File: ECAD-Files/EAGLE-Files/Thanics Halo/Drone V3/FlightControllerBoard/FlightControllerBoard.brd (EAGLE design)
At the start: 60 x 80 mm, 92 parts, among them J12 UE27AE54100, J4 UE27AE54100, J5 U.FL, J7 62674-301121ALF, J8 MICROSD, U3 MPL115A2, U4 NEO-M8, U5 VL53L1

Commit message: Finished overall board zoning and component placement
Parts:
- removed C19, C22, C7, C8: 16pF, 16pF-capacitor:G-155-M
- removed J6: (no value), thanics_robotics:JST_SH_2POS
- removed R32: 20R, 20-resistor:RC0603N-M
- removed U5: VL53L1, thanics_robotics:VL53L1
- added C1, C12: 0.1uF, 0.1uF-capacitor-0402:0402-M
- added D2, D3, D4: GREEN, SparkFun-LED:LED-0603
- added J10, J11, J15, J16, J17, J18, J19, J20, J21, J22, J9: (no value), thanics_robotics:JST_SH_4POS
- added JP1: (no value), pinhead:2X06
- added L4: 1000R, 600ohm-fb:IND_BLM18_0603-M
- added R24, R25, R26, R27: 49R9, 49.9-resistor:RC0402N-M
- added R28, R30, R31: 1k, 1k-resistor:RC0603N-M
- added R29: 10k, 10k-resistor(0603):RC0603N-M
- C41: value 0.1uF -> 22uF; device 0.1uF-capacitor-0402:0402-M -> 22uF X5R Ceramic Capacitor:G-21
- C42: value 4.7uF -> 10uF; device 4.7uF-capacitor:0603-M -> 10uF X5R Ceramic Capacitor:G-21
- R10, R11, R13, R14, R2: device 10k-resistor:RC0805N -> 10k-resistor(0603):RC0603N-M
- R19: value 10k -> 1k; device 10k-resistor:RC0805N -> 1k-resistor:RC0603N-M
- moved R10 364.1 mm to (-86.3, -281.3)
- moved R13 360.1 mm to (-86.3, -278.4)
- moved R11 357.8 mm to (-86.3, -275.5)
- moved J1 308.4 mm to (4.32, 68.8)
- moved J2 294.7 mm to (4.37, 63.4)
- moved U$2 293.6 mm to (24.4, 44.6), turned to 180 degrees
- moved R2 201.8 mm to (-86.3, -272.6)
- moved C16 158.5 mm to (37.5, 30.1), flipped to the bottom
- moved R20 158.2 mm to (32.3, 32.4), flipped to the bottom, turned to 315 degrees
- moved C15 157.9 mm to (36.6, 26.2)
- moved R21 152.5 mm to (28.8, 31.9), flipped to the bottom, turned to 225 degrees
- moved C17 150.8 mm to (32.5, 27.8), turned to 90 degrees
- moved C25 146.6 mm to (30.2, 27.8), turned to 90 degrees
- moved R4 140.8 mm to (26.8, 29.1)
- moved C6 139.8 mm to (34.3, 26.5), turned to 90 degrees
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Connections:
- removed net BATT_SCL: J7.20
- removed net BATT_SDA: J7.19
- removed net GPCLK: U2.61
- removed net N$17: U6.60
- new net ETH_BIAS: C1.2, L4.2, U$1.13
- new net GND1: D2.C, U$1.60
- new net GND2: D3.C
- new net GPIO12: JP1.1, U6.45
- new net GPIO13: JP1.3, U6.47
- new net GPIO16: JP1.5, U6.57
- new net GPIO17: JP1.2, U6.59
- new net GPIO37: JP1.4, U6.60
- new net GPIO38: JP1.6, U6.64
- new net GPIO39: JP1.8, U6.66
- new net N$22: D3.A, R30.1
- new net N$23: C12.2, L4.1, R24.1, R25.1, R26.1, R27.1
- new net N$24: R2.2, U$1.15
- new net N$25: D4.A, U$1.11
- new net N$27: D4.C, R31.1
- net +3V3: now also C42.1, J10.1, J11.1, J15.1, J16.1, J17.1, J18.1, J19.1, J20.1, J21.1, J22.1, J9.1, JP1.11, R19.2, R29.2, R30.2, U$1.61, U$1.62, U$2.16, U$2.6; no longer C41.2, C42.2, R19.1, R2.2, R32.2, U5.1, U5.11
- net +5V: now also C41.1, JP1.12, U$1.63, U$1.64; no longer J6.1
- net 3.3V_A: now also R2.1, R28.2
- net GND: now also C1.1, C12.1, C41.2, C42.2, J10.4, J11.4, J15.4, J16.4, J17.4, J18.4, J19.4, J20.4, J21.4, J22.4, J9.4, JP1.10, R31.2, U$1.1, U$1.17, U$1.25, U$1.26, U$1.39, U$1.40, U$2.7, U$2.8; no longer C19.1, C22.1, C41.1, C42.1, C7.1, C8.1, J6.2, U5.12, U5.2, U5.3, U5.4, U5.6
- net GPCLK1: now also U2.61
- net I2C_SCL: now also J10.3, J11.3, J15.3, J16.3, J17.3, J18.3, J19.3, J20.3, J21.3, J22.3, J7.20, J9.3, JP1.7; no longer U5.10
- net I2C_SDA: now also J10.2, J11.2, J15.2, J16.2, J17.2, J18.2, J19.2, J20.2, J21.2, J22.2, J7.19, J9.2, JP1.9; no longer U5.9
- net N$12: now also D2.A, R28.1; no longer R19.2, U5.5
- net N$3: now also R29.1; no longer R2.1
- net N$4: now also R19.1; no longer R32.1
- net NRST: now also U$2.4
- net NRST1: now also U$2.5
- net NRST2: now also U$2.3
- net RX_LAN_N: now also R25.2
- net RX_LAN_P: now also R26.2
- net RX_N: no longer C7.2
- net RX_P: no longer C19.2
- net SEL2: now also U$2.10, U$2.11, U$2.9
- net SWCLK: now also U$2.15
- net SWCLK1: now also U$2.2
- net SWCLK2: now also U$2.1
- net SWDIO: now also U$2.14
- net SWDIO1: now also U$2.12
- net SWDIO2: now also U$2.13
- net TX_LAN_N: now also R27.2
- net TX_LAN_P: now also R24.2
- net TX_N: no longer C22.2
- net TX_P: no longer C8.2
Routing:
- net SDX_D3: track 36.8 -> 11.9 mm
- net SDX_D2: track 37.0 -> 12.8 mm
- net C1_C_P: track 7.33 -> 0.00 mm
- net C1_C_N: track 7.32 -> 0.00 mm
- net C1_D1_N: track 6.12 -> 0.00 mm
- net C1_D1_P: track 6.07 -> 0.00 mm
- net C1_D0_P: track 5.12 -> 0.00 mm
- net C1_D0_N: track 5.11 -> 0.00 mm
- net TX_LAN_P: track 3.57 -> 7.91 mm
- net TX_P: track 7.76 -> 4.14 mm
- net TX_N: track 7.77 -> 4.34 mm
- net TX_LAN_N: track 4.16 -> 7.19 mm, vias 0 -> 2
- net SDX_CMD: track 35.3 -> 37.9 mm
- net SDX_D1: track 37.8 -> 40.4 mm
- net SDX_D0: track 37.4 -> 39.9 mm
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
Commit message: Repositioned ethernet pullup resistors
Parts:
- removed C3: 0.1uF, 0.1uF X7R Ceramic Capacitor:0805
- added C7: 0.1uF, 0.1uF-capacitor-0402:0402-M
- C2: device 0.1uF X7R Ceramic Capacitor:0805 -> 0.1uF-capacitor-0402:0402-M
- moved C1 298.4 mm to (25.0, 41.9), turned to 180 degrees
- moved C12 297.2 mm to (22.6, 38.6)
- moved L4 282.6 mm to (23.0, 40.8), turned to 90 degrees
- moved C43 269.1 mm to (53.3, 18.5), flipped to the bottom
- moved C40 257.4 mm to (10.5, 75.4)
- moved C39 254.5 mm to (8.51, 76.2), turned to 90 degrees
- moved C24 151.3 mm to (54.1, 26.3), turned to 90 degrees
- moved R22 148.7 mm to (29.0, 30.6), flipped to the bottom, turned to 45 degrees
- moved R23 147.6 mm to (30.2, 31.8), flipped to the bottom, turned to 45 degrees
- moved C11 147.0 mm to (41.7, 55.8), turned to 90 degrees
- moved C9 146.1 mm to (37.8, 54.9), turned to 180 degrees
- moved C2 99.6 mm to (39.5, 64.1)
- moved C37 2.33 mm to (29.7, 34.5)
- moved C38 2.33 mm to (30.4, 35.2)
- moved R21 2.19 mm to (30.9, 32.5), turned to 45 degrees
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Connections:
- net +3V3: now also C7.2; no longer C3.2
- net GND: now also C7.1; no longer C3.1
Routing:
- net SDX_D2: track 12.8 -> 6.50 mm
- net SDX_D3: track 11.9 -> 6.74 mm
- net TX_N: track 4.34 -> 6.94 mm
- net TX_P: track 4.14 -> 6.62 mm
- net RX_LAN_P: track 3.87 -> 5.31 mm
- net RX_LAN_N: track 3.87 -> 5.31 mm
- net TX_LAN_N: track 7.19 -> 6.19 mm
- net TX_LAN_P: track 7.91 -> 6.94 mm

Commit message: Routed more traces, recognized that PowerSwitchingBoard connector needs to be reversed
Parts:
- removed D3: GREEN, SparkFun-LED:LED-0603
- removed JP1: (no value), pinhead:2X06
- removed R11, R13: 10k, 10k-resistor(0603):RC0603N-M
- removed R30: 1k, 1k-resistor:RC0603N-M
- removed R45: 10k, 10k-resistor:RC0805N
- added R32: 10k, 10k-resistor(0603):RC0603N-M
- moved R2 367.4 mm to (34.5, 74.4), flipped to the bottom, turned to 180 degrees
- moved R31 363.6 mm to (23.0, 77.1), turned to 270 degrees
- moved D4 357.1 mm to (24.5, 77.0), turned to 90 degrees
- moved R10 339.4 mm to (20.4, 40.9)
- moved R19 337.3 mm to (26.5, 77.1), turned to 90 degrees
- moved C42 310.6 mm to (20.8, 36.4), flipped to the bottom, turned to 270 degrees
- moved C41 305.7 mm to (18.2, 36.4), flipped to the bottom, turned to 270 degrees
- moved R28 296.7 mm to (5.08, 35.2)
- moved D2 292.2 mm to (4.95, 33.7)
- moved C34 154.3 mm to (39.1, 54.7)
- moved R15 101.6 mm to (9.53, 31.9), flipped to the bottom, turned to 270 degrees
- moved C21 82.6 mm to (31.1, 67.2)
- moved D1 70.0 mm to (27.9, 77.0), turned to 90 degrees
- moved C10 68.0 mm to (20.3, 67.7), turned to 180 degrees
- moved R18 62.9 mm to (4.45, 24.6), flipped to the bottom, turned to 180 degrees
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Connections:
- removed net GND2: D3.C
- removed net N$22: D3.A, R30.1
- net +3V3: now also R2.1; no longer JP1.11, R30.2
- net +5V: no longer JP1.12
- net 3.3V_A: no longer R2.1
- net GND: now also R32.2; no longer JP1.10, R11.2, R13.2, R45.2
- net GPIO12: no longer JP1.1
- net GPIO13: no longer JP1.3
- net GPIO16: no longer JP1.5
- net GPIO17: no longer JP1.2
- net GPIO37: no longer JP1.4
- net GPIO38: no longer JP1.6
- net GPIO39: no longer JP1.8
- net I2C_SCL: no longer JP1.7
- net I2C_SDA: no longer JP1.9
- net N$53: now also R32.1; no longer R45.1
- net SCL0: no longer R11.1
- net SDA0: no longer R13.1
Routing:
- net +3V3: track 0.00 -> 179.1 mm, vias 0 -> 5
- net 1.8V: track 0.00 -> 91.1 mm, vias 0 -> 2
- net I2C_SDA: track 0.00 -> 79.9 mm, vias 0 -> 2
- net I2C_SCL: track 0.00 -> 72.9 mm, vias 0 -> 2
- net BOOT0: track 0.00 -> 60.3 mm, vias 0 -> 2
- net +5V: track 0.00 -> 54.1 mm, vias 0 -> 1
- net SCK: track 0.00 -> 53.5 mm, vias 0 -> 2
- net MISO: track 0.00 -> 50.3 mm, vias 0 -> 2
- net MOSI: track 0.00 -> 49.9 mm, vias 0 -> 2
- net RST: track 0.00 -> 45.8 mm, vias 0 -> 2
- net SEL1: track 0.00 -> 40.0 mm, vias 0 -> 2
- net SWDIO2: track 0.00 -> 39.3 mm, vias 0 -> 2
- net SEL0: track 0.00 -> 38.4 mm, vias 0 -> 2
- net SWCLK2: track 0.00 -> 36.3 mm, vias 0 -> 2
- net NRST2: track 0.00 -> 36.1 mm, vias 0 -> 2
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- added copper zone on layer 1, net GND
- added copper zone on layer 16, net GND

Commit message: Finished Power Switching Board and Flight Controller Board v1
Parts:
- added JP1: (no value), pinhead:1X01
- L4: value 1000R -> 1k@100MHz
- moved D2 46.7 mm to (38.5, 1.24), turned to 180 degrees
- moved R28 46.6 mm to (38.5, 2.62), turned to 180 degrees
- moved R2 6.98 mm to (38.1, 68.4), flipped to the top, turned to 0 degrees
- moved R6 4.64 mm to (32.6, 40.4), turned to 180 degrees
- moved R7 4.54 mm to (32.6, 38.5)
- moved R9 4.54 mm to (32.6, 34.4)
- moved R3 4.54 mm to (32.6, 44.5)
- moved R5 4.54 mm to (32.6, 42.4)
- moved R8 4.54 mm to (32.6, 36.6)
- moved U11 4.47 mm to (45.8, 39.7)
- moved C20 2.69 mm to (34.9, 49.5)
- moved C5 2.39 mm to (22.1, 53.8)
- moved R10 1.40 mm to (19.4, 40.0), turned to 270 degrees
- moved R24 1.40 mm to (29.2, 39.6)
- moved R27 1.40 mm to (27.8, 39.6)
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- renumbered U$1 to U7, U$2 to U8
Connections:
- removed net FAULT: J7.27
- net GEAR: now also JP1.1
- net GND: now also J7.27
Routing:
- net +3V3: track 179.1 -> 295.9 mm, vias 5 -> 32
- net ID_SD: track 0.00 -> 105.9 mm, vias 0 -> 6
- net +5V: track 54.1 -> 133.9 mm, vias 1 -> 3
- net I2C_SDA: track 79.9 -> 143.9 mm, vias 2 -> 8
- net I2C_SCL: track 72.9 -> 136.4 mm, vias 2 -> 10
- net UART2_RX: track 0.00 -> 62.6 mm, vias 0 -> 4
- net SEL2: track 0.00 -> 56.9 mm, vias 0 -> 6
- net ETH_BIAS: track 0.00 -> 53.3 mm, vias 0 -> 3
- net UART2_TX: track 0.00 -> 52.2 mm, vias 0 -> 4
- net SCL1: track 0.00 -> 49.0 mm, vias 0 -> 2
- net SDA1: track 0.00 -> 48.8 mm, vias 0 -> 2
- net GND1: track 0.00 -> 47.8 mm, vias 0 -> 1
- net USART1_RX: track 20.8 -> 65.8 mm, vias 1 -> 3
- net SDX_D3: track 1.27 -> 44.4 mm, vias 0 -> 2
- net SDX_D2: track 1.44 -> 43.7 mm, vias 0 -> 2
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- added copper zone on layer 2, net +3V3
- added copper zone on layer 15, net GND
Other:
- board text added: "*Made on Earth by humans*"
- board text added: "3V3"
- board text added: "CAM0"
- board text added: "CAM1"
- board text added: "ETH"
- board text added: "Flight Controller Board v1"
- board text added: "GPS Antenna"
- board text added: "RADIO"
- board text added: "SD Card"
- board text added: "TELEMETRY"
- board text added: "To Power Board ->"

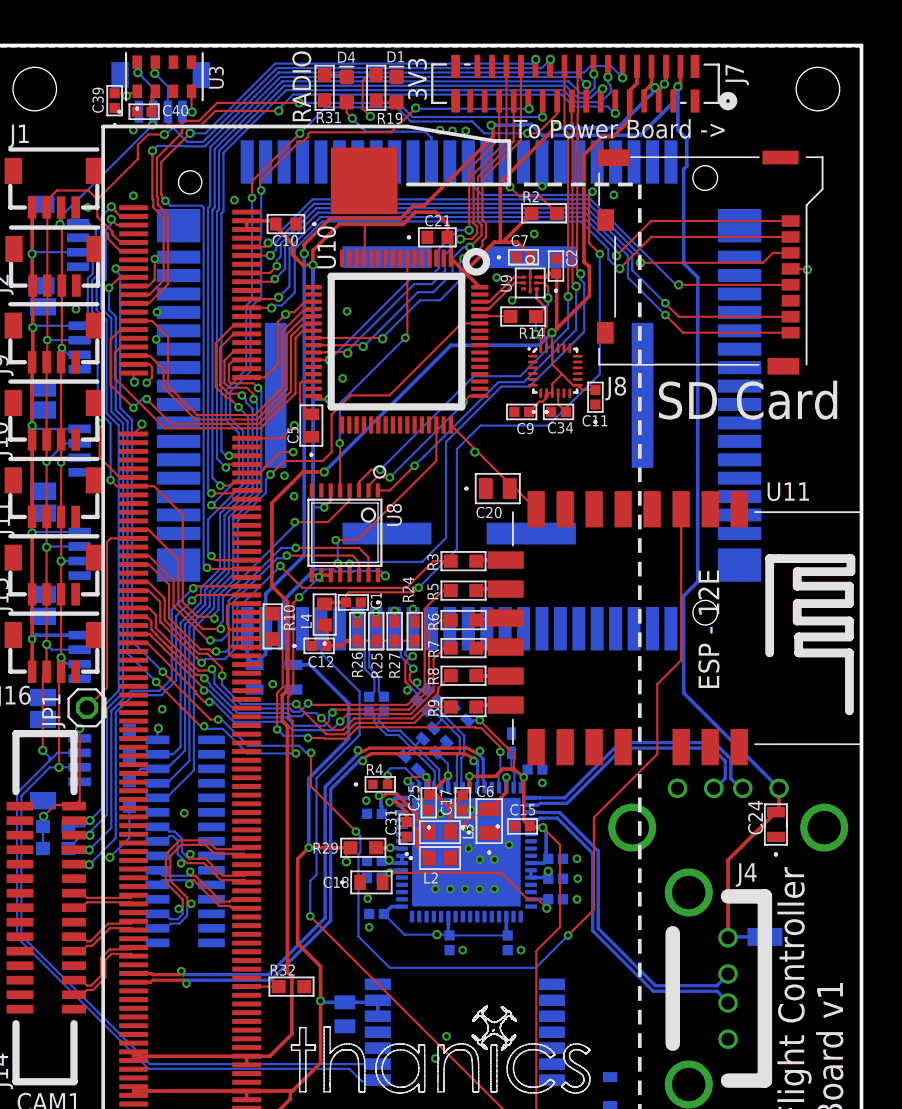
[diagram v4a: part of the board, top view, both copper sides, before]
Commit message: Changed ethernet capacitor isolation to transformers
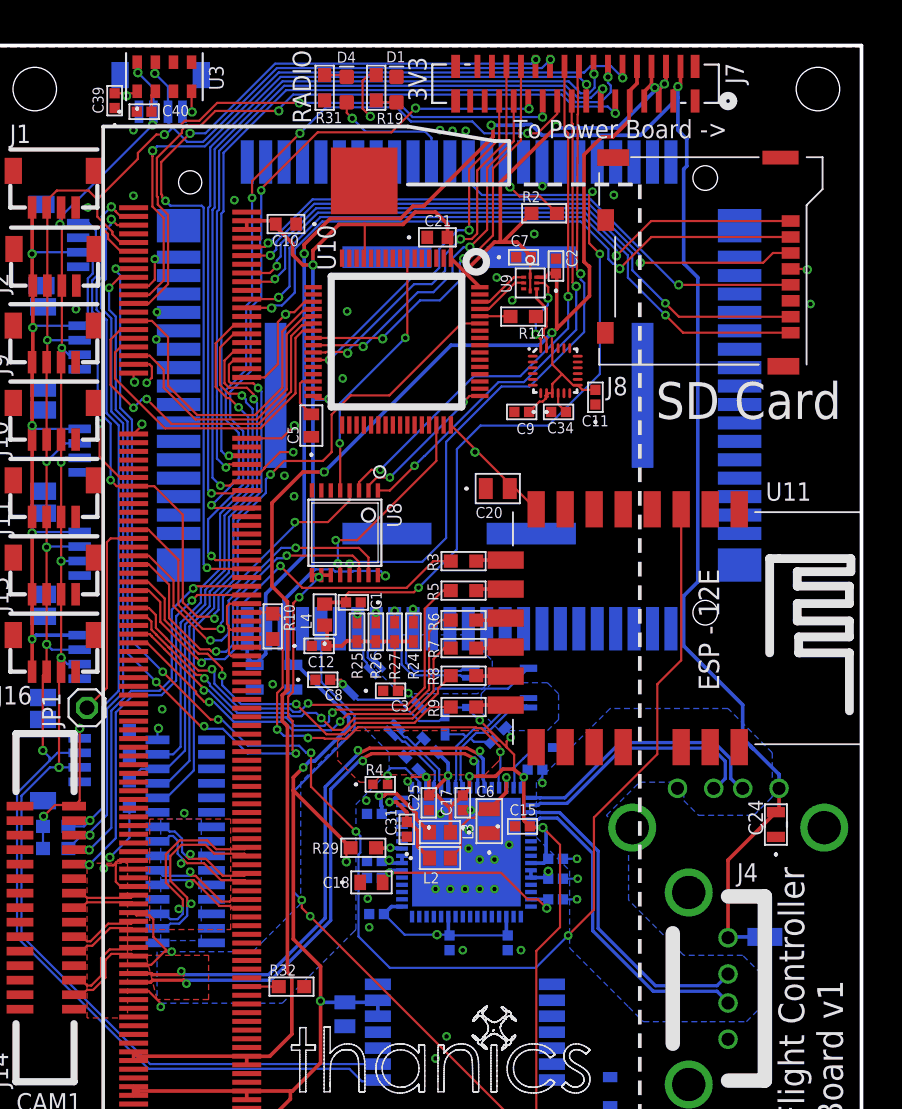
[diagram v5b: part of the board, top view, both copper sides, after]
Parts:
- removed C23, C36, C37, C38: 0.1uF, 0.1uF-capacitor-0402:0402-M
- added C3, C8: 0.1uF, 0.1uF-capacitor-0402:0402-M
- added T1, T2: ALT4532M, thanics_robotics:ALT4532
- R12: value 10 -> 10R
- moved R20 2.98 mm to (35.0, 32.5), turned to 315 degrees
- moved R1 2.31 mm to (38.2, 31.6), turned to 180 degrees
- moved R23 1.80 mm to (30.3, 31.8)
- moved R22 1.72 mm to (29.0, 30.5)
- moved R25 1.32 mm to (25.2, 39.6)
- moved R26 1.27 mm to (26.5, 39.6)
- moved R21 0.80 mm to (31.3, 33.2), turned to 270 degrees
- moved R24 0.11 mm to (29.1, 39.6)
- moved R27 0.05 mm to (27.8, 39.6)
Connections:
- net BOOT0 renamed PWR_EN
- net +3V3: no longer U8.6
- net 3.3V_A: now also C8.2, T1.3, T2.3
- net GND: now also C3.1, C8.1, U8.6
- net N$23: now also C3.2, T1.6, T2.6
- net RX_LAN_N: now also R26.2, T1.1; no longer C36.2, R25.2
- net RX_LAN_P: now also R25.2, T1.2; no longer C23.2, R26.2
- net RX_N: now also R23.2, T1.5; no longer C36.1, R22.2
- net RX_P: now also R22.2, T1.4; no longer C23.1, R23.2
- net TX_LAN_N: now also T2.2; no longer C38.2
- net TX_LAN_P: now also T2.1; no longer C37.2
- net TX_N: now also T2.4; no longer C38.1
- net TX_P: now also T2.5; no longer C37.1
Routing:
- net GND: track 16.8 -> 35.3 mm, vias 48 -> 52
- net N$23: track 7.75 -> 21.9 mm, vias 0 -> 1
- net 3.3V_A: track 62.1 -> 75.0 mm, vias 7 -> 9
- net TX_P: track 7.48 -> 10.9 mm
- net RX_P: track 8.44 -> 5.99 mm
- net TX_N: track 7.86 -> 10.3 mm
- net RX_LAN_N: track 7.04 -> 4.92 mm
- net RX_N: track 8.43 -> 6.32 mm
- net RX_LAN_P: track 6.83 -> 4.91 mm
- net TX_LAN_N: track 8.15 -> 9.83 mm, vias 3 -> 1
- net N$5: track 2.52 -> 3.40 mm
- net GND1: track 47.8 -> 48.5 mm, vias 1 -> 2
- net UART2_TX: track 52.2 -> 51.6 mm
- net +3V3: track 295.9 -> 296.3 mm, vias 32 -> 31
- net TX_LAN_P: track 9.22 -> 9.64 mm, vias 3 -> 1
- added copper zone on layer 1, net N$17
- added copper zone on layer 1, net N$22
- added copper zone on layer 1, net N$28
- added copper zone on layer 16, net N$29
- added copper zone on layer 16, net N$30
- added copper zone on layer 16, net N$31
- added copper zone on layer 16, net N$32
- added copper zone on layer 16, net N$33
- added copper zone on layer 1, net N$34

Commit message: Created TOF Altimeter Board v1, and made power board 4 layers
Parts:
- added C62, C67: 10uF, 10uF X5R Ceramic Capacitor:G-21
- added C65, C66: 0.1uF, 0.1uF-capacitor-0402:0402-M
- added U5: AZ1117EH-1.8, thanics_robotics:SOT-223
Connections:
- net +5V: now also C62.2, C65.2, U5.3
- net 1.8V: now also C66.2, C67.2, U5.2, U5.4; no longer J7.7, J7.8
- net GND: now also C62.1, C65.1, C66.1, C67.1, J7.7, J7.8, U5.1
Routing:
- net +5V: track 133.9 -> 153.0 mm, vias 3 -> 4
- net 3.3V_A: track 75.0 -> 80.6 mm, vias 9 -> 11
- net 1.8V: track 111.8 -> 108.0 mm, vias 2 -> 4
- net GND1: track 48.5 -> 51.8 mm, vias 2 -> 1
- net GND: vias 52 -> 51
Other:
- board text added: "Flight Controller Board v1.1"
- board text removed: "Flight Controller Board v1"
